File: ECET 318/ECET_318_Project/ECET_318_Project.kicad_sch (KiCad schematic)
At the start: 8 parts, among them J1 Screw_Terminal_01x02, J2 Screw_Terminal_01x03, J3 Screw_Terminal_01x02

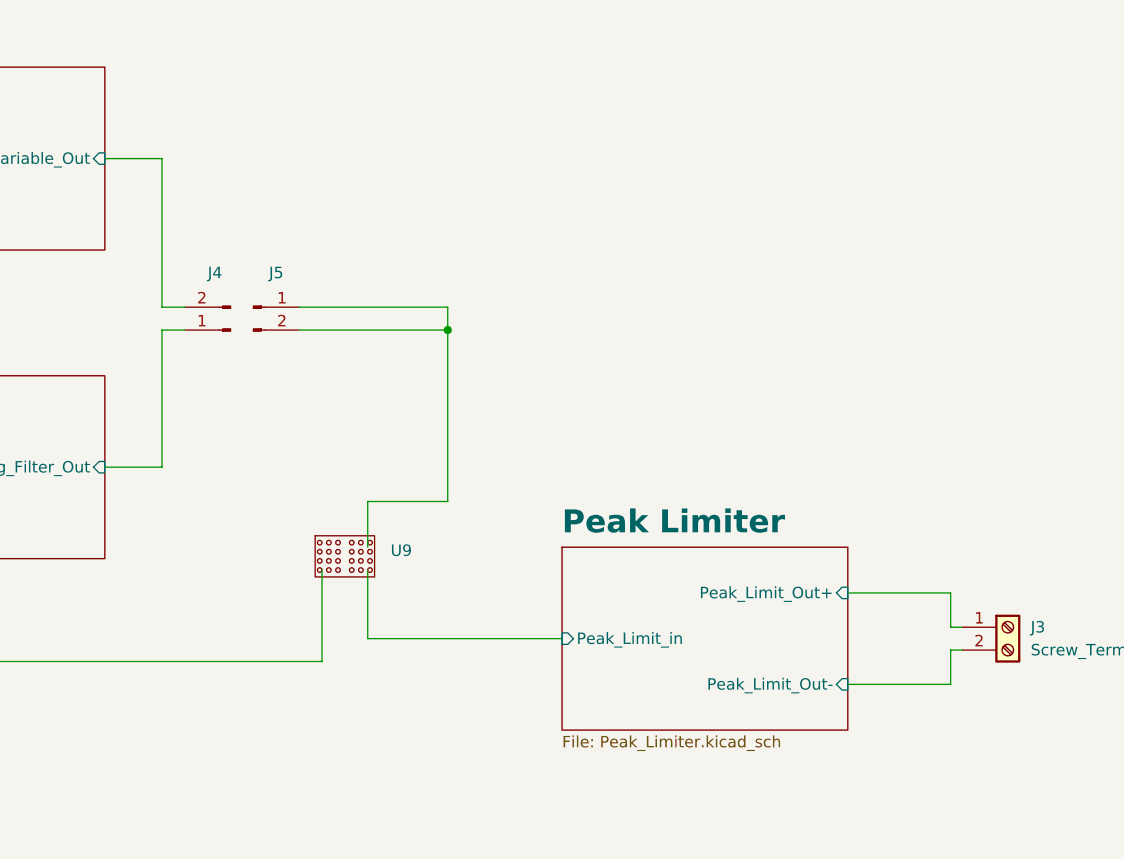
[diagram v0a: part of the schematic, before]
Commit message: Mostly finished Layout and change U5 to TL084
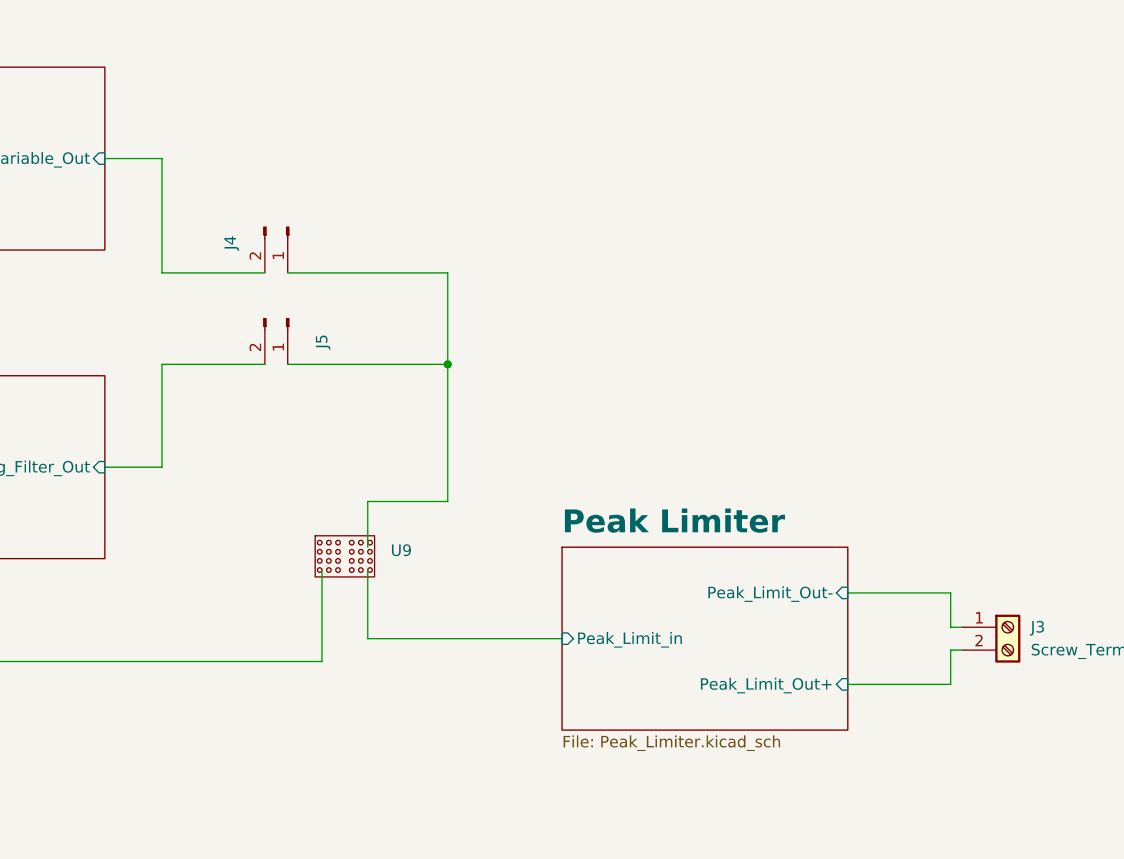
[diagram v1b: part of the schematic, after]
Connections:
- net Peak Limiter/Peak_Limit_Out+: now also J3.2 (Pin_2); no longer J3.1 (Pin_1)
- net Peak Limiter/Peak_Limit_Out-: now also J3.1 (Pin_1); no longer J3.2 (Pin_2)
- net Shelving Filter/Shelving_Filter_Out: now also J5.2 (Pin_2); no longer J4.1 (Pin_1)
- net at J5.1 (Pin_1): now also J4.1 (Pin_1); no longer J5.2 (Pin_2)
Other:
- moved on the sheet: J4, J5

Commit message: Roughly finished component placeament and routing
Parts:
- removed U9: ~, Custom_parts:BreadBoard Space, symbol Custom_parts:BreadBoard_Space
- added U6: ~, Custom_parts:800CSP1B6M2QE, symbol Custom_parts:SPDT_Latching_Pushbutton
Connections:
- net Mic Amp/Mic_Amp_Out: now also U6.3
- net Peak Limiter/Peak_Limit_in: now also U6.2
- net at J4.1 (Pin_1), J5.1 (Pin_1): now also U6.1
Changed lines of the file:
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@@
 	(paper "A3")
-	(junction
-		(at 218.44 88.9)
-		(diameter 0)
-		(color 0 0 0 0)
-	)
 	(junction
 		(at 129.54 121.92)
@@
 		(color 0 0 0 0)
 	)
+	(junction
+		(at 210.82 88.9)
+		(diameter 0)
+		(color 0 0 0 0)
+	)
 	(wire
 		(pts
@@
 	(wire
 		(pts
-			(xy 204.47 111.76) (xy 204.47 121.92)
-		)
-		(stroke
-			(width 0)
-			(type default)
-		)
-	)
-	(wire
-		(pts
 			(xy 52.07 228.6) (xy 52.07 232.41)
 		)
@@
 	(wire
 		(pts
+			(xy 226.06 119.38) (xy 231.14 119.38)
+		)
+		(stroke
+			(width 0)
+			(type default)
+		)
+	)
+	(wire
+		(pts
 			(xy 104.14 121.92) (xy 129.54 121.92)
 		)
@@
 	(wire
 		(pts
-			(xy 209.55 104.14) (xy 209.55 109.22)
-		)
-		(stroke
-			(width 0)
-			(type default)
-		)
-	)
-	(wire
-		(pts
-			(xy 218.44 78.74) (xy 218.44 88.9)
+			(xy 210.82 78.74) (xy 210.82 88.9)
 		)
 		(stroke
@@
 	(wire
 		(pts
-			(xy 209.55 111.76) (xy 209.55 119.38)
-		)
-		(stroke
-			(width 0)
-			(type default)
-		)
-	)
-	(wire
-		(pts
 			(xy 180.34 66.04) (xy 186.69 66.04)
 		)
@@
 	(wire
 		(pts
-			(xy 129.54 121.92) (xy 204.47 121.92)
-		)
-		(stroke
-			(width 0)
-			(type default)
-		)
-	)
-	(wire
-		(pts
-			(xy 218.44 88.9) (xy 218.44 104.14)
+			(xy 129.54 121.92) (xy 213.36 121.92)
 		)
 		(stroke
@@
 	(wire
 		(pts
+			(xy 210.82 116.84) (xy 210.82 88.9)
+		)
+		(stroke
+			(width 0)
+			(type default)
+		)
+	)
+	(wire
+		(pts
+			(xy 213.36 116.84) (xy 210.82 116.84)
+		)
+		(stroke
+			(width 0)
+			(type default)
+		)
+	)
+	(wire
+		(pts
 			(xy 275.59 118.11) (xy 274.32 118.11)
 		)
@@
 	(wire
 		(pts
-			(xy 218.44 104.14) (xy 209.55 104.14)
-		)
-		(stroke
-			(width 0)
-			(type default)
-		)
-	)
-	(wire
-		(pts
-			(xy 200.66 88.9) (xy 218.44 88.9)
+			(xy 200.66 88.9) (xy 210.82 88.9)
 		)
 		(stroke
@@
 	(wire
 		(pts
-			(xy 231.14 119.38) (xy 209.55 119.38)
-		)
-		(stroke
-			(width 0)
-			(type default)
-		)
-	)
-	(wire
-		(pts
 			(xy 59.69 120.65) (xy 67.31 120.65)
 		)
@@
 	(wire
 		(pts
-			(xy 200.66 78.74) (xy 218.44 78.74)
+			(xy 200.66 78.74) (xy 210.82 78.74)
 		)
 		(stroke
@@
 	)
 	(symbol
-		(lib_id "Custom_parts:BreadBoard_Space")
-		(at 207.01 110.49 0)
-		(unit 1)
-		(exclude_from_sim no)
-		(in_bom yes)
-		(on_board yes)
-		(dnp no)
-		(fields_autoplaced yes)
-		(property "Reference" "U9"
-			(at 212.09 109.6009 0)
-			(effects
-				(font
-					(size 1.27 1.27)
-				)
-				(justify left)
-			)
-		)
-		(property "Value" "~"
-			(at 212.09 111.506 0)
-			(effects
-				(font
-					(size 1.27 1.27)
-				)
-				(justify left)
-			)
-		)
-		(property "Footprint" "Custom_parts:BreadBoard Space"
-			(at 207.01 110.49 0)
-			(effects
-				(font
-					(size 1.27 1.27)
-				)
-				(hide yes)
-			)
-		)
-		(property "Datasheet" ""
-			(at 207.01 110.49 0)
-			(effects
-				(font
-					(size 1.27 1.27)
-				)
-				(hide yes)
-			)
-		)
-		(property "Description" ""
-			(at 207.01 110.49 0)
-			(effects
-				(font
-					(size 1.27 1.27)
-				)
-				(hide yes)
-			)
-		)
-		(instances
-			(project ""
-				(path "/f1e8215e-2100-40b3-b836-5691fd657e21"
-					(reference "U9")
-					(unit 1)
-				)
-			)
-		)
-	)
-	(symbol
 		(lib_id "power:+15V")
 		(at 52.07 228.6 0)
@@
 					(unit 1)
 				)
+			)
+		)
+	)
+	(symbol
+		(lib_id "Custom_parts:SPDT_Latching_Pushbutton")
+		(at 219.71 116.84 0)
+		(unit 1)
+		(exclude_from_sim no)
+		(in_bom yes)
+		(on_board yes)
+		(dnp no)
+		(property "Reference" "U6"
+			(at 219.71 111.506 0)
+			(effects
+				(font
+					(size 1.27 1.27)
+				)
+			)
+		)
+		(property "Value" "~"
+			(at 219.71 110.49 0)
+			(effects
+				(font
+					(size 1.27 1.27)
+				)
+			)
+		)
+		(property "Footprint" "Custom_parts:800CSP1B6M2QE"
+			(at 219.71 116.84 0)
+			(effects
+				(font
+					(size 1.27 1.27)
+				)
+				(hide yes)
+			)
+		)
+		(property "Datasheet" ""
+			(at 219.71 116.84 0)
+			(effects
+				(font
+					(size 1.27 1.27)
+				)
+				(hide yes)
+			)
+		)
+		(property "Description" ""
+			(at 219.71 116.84 0)
+			(effects
+				(font
+					(size 1.27 1.27)
+				)
+				(hide yes)
+			)
+		)
+		(pin "3"
+		)
+		(pin "1"
+		)
+		(pin "2"
+		)
+		(instances
+			(project ""
+				(path "/f1e8215e-2100-40b3-b836-5691fd657e21"
+					(reference "U6")
+					(unit 1)
+				)

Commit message: Added Breadboard Space and Test Points
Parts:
- added J10, J11, J6, J7, J8, J9: Conn_01x01_Socket, TestPoint:TestPoint_THTPad_D1.5mm_Drill0.7mm, symbol Connector:Conn_01x01_Socket
- added TP2: TestPoint_Flag, TestPoint:TestPoint_Pad_D1.5mm, symbol Connector:TestPoint_Flag
- added U7, U8, U9: ~, Custom_parts:BreadBoard Space, symbol Custom_parts:BreadBoard_Space
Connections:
- net +15V: now also J6.1 (Pin_1), J9.1 (Pin_1)
- net -15V: now also J11.1 (Pin_1), J8.1 (Pin_1)
- net GND: now also J10.1 (Pin_1), J7.1 (Pin_1)
- net Peak Limiter/Peak_Limit_in: now also TP2.1
